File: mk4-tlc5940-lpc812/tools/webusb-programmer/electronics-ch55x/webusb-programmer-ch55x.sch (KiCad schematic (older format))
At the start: 19 parts, among them J1 USB_B_Micro, J2 Light Controller, Q1 PMV30UN, U1 CH552G, U3 STMPS2141STR

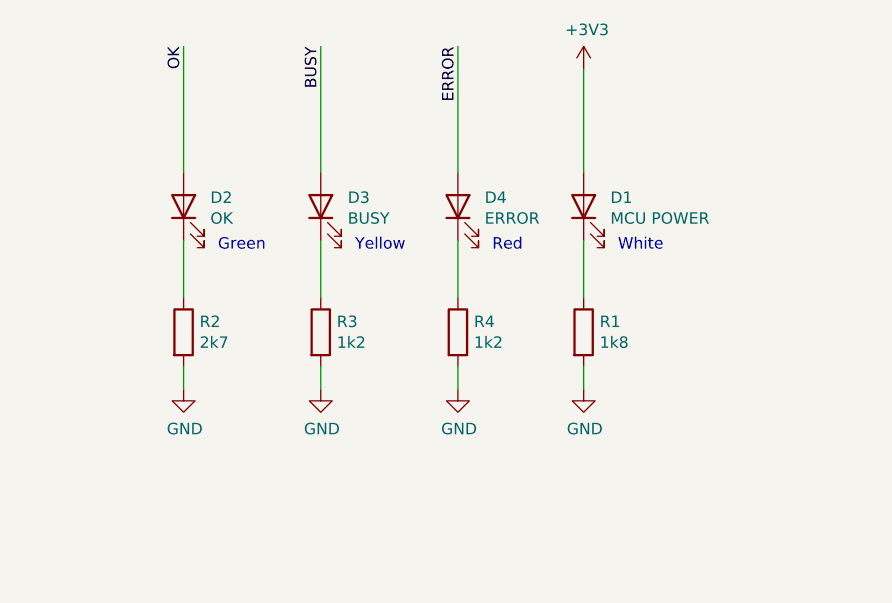
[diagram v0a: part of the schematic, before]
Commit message: Reverse LED polarity to prevent pull-up from lighting them up
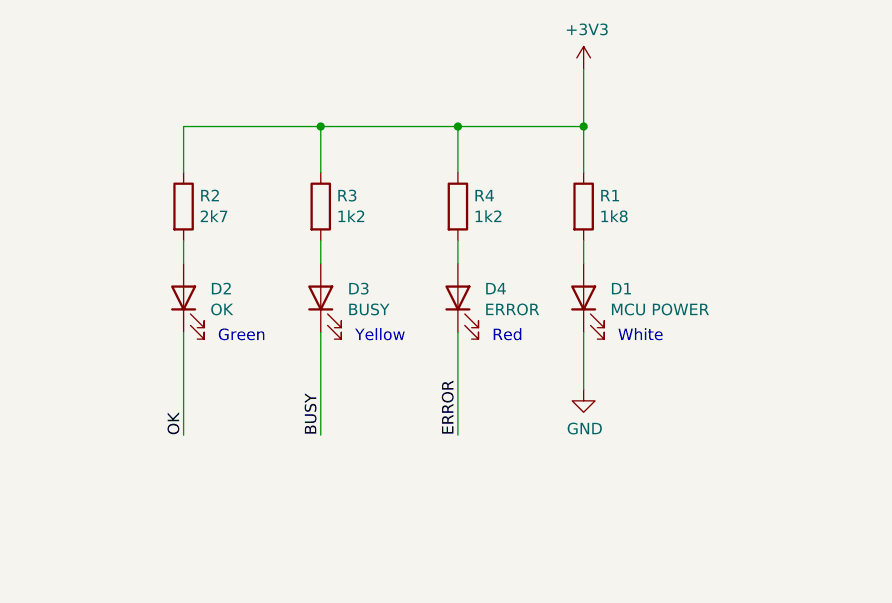
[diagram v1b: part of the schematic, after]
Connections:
- net +3V3: now also R1.1, R2.1, R3.1, R4.1; no longer D1.2 (A)
- net BUSY: now also D3.1 (K); no longer D3.2 (A)
- net ERROR: now also D4.1 (K); no longer D4.2 (A)
- net GND: now also D1.1 (K); no longer R1.2, R2.2, R3.2, R4.2
- net OK: now also D2.1 (K); no longer D2.2 (A)
- new net: D2.2 (A), R2.2
- new net: D3.2 (A), R3.2
- new net: D4.2 (A), R4.2
- new net: D1.2 (A), R1.2
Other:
- moved on the sheet: D1, D2, D3, D4, R1, R2, R3, R4
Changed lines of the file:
@@
 L Device:LED D2
 U 1 1 5E6F6F74
-P 3150 1800
-F 0 "D2" V 3189 1683 50  0000 R CNN
-F 1 "OK" V 3098 1683 50  0000 R CNN
-F 2 "WLA_LED_reverse_mount:LED_1204_reverse_mout" H 3150 1800 50  0001 C CNN
-F 3 "2011131907_TUOZHAN-TZ-P2-1204YGCTA1-1-5T" H 3150 1800 50  0001 C CNN
-F 4 "C91608" V 3150 1800 50  0001 C CNN "LCSC part number"
-	1    3150 1800
+P 3150 2200
+F 0 "D2" V 3189 2083 50  0000 R CNN
+F 1 "OK" V 3098 2083 50  0000 R CNN
+F 2 "WLA_LED_reverse_mount:LED_1204_reverse_mout" H 3150 2200 50  0001 C CNN
+F 3 "2011131907_TUOZHAN-TZ-P2-1204YGCTA1-1-5T" H 3150 2200 50  0001 C CNN
+F 4 "C91608" V 3150 2200 50  0001 C CNN "LCSC part number"
+	1    3150 2200
 	0    -1   -1   0
 $EndComp
@@
 L Device:LED D3
 U 1 1 5E6F790B
-P 3750 1800
-F 0 "D3" V 3789 1682 50  0000 R CNN
-F 1 "BUSY" V 3698 1682 50  0000 R CNN
-F 2 "WLA_LED_reverse_mount:LED_1204_reverse_mout" H 3750 1800 50  0001 C CNN
-F 3 "2009041237_TUOZHAN-TZ-P2-1204-0TA1-1-5T" H 3750 1800 50  0001 C CNN
-F 4 "C779805" V 3750 1800 50  0001 C CNN "LCSC part number"
-	1    3750 1800
+P 3750 2200
+F 0 "D3" V 3789 2082 50  0000 R CNN
+F 1 "BUSY" V 3698 2082 50  0000 R CNN
+F 2 "WLA_LED_reverse_mount:LED_1204_reverse_mout" H 3750 2200 50  0001 C CNN
+F 3 "2009041237_TUOZHAN-TZ-P2-1204-0TA1-1-5T" H 3750 2200 50  0001 C CNN
+F 4 "C779805" V 3750 2200 50  0001 C CNN "LCSC part number"
+	1    3750 2200
 	0    -1   -1   0
 $EndComp
@@
 L Device:LED D4
 U 1 1 5E6F7DEF
-P 4350 1800
-F 0 "D4" V 4389 1683 50  0000 R CNN
-F 1 "ERROR" V 4298 1683 50  0000 R CNN
-F 2 "WLA_LED_reverse_mount:LED_1204_reverse_mout" H 4350 1800 50  0001 C CNN
-F 3 "1905151403_MEIHUA-MHS110KECT" H 4350 1800 50  0001 C CNN
-F 4 "C389527" V 4350 1800 50  0001 C CNN "LCSC part number"
-	1    4350 1800
+P 4350 2200
+F 0 "D4" V 4389 2083 50  0000 R CNN
+F 1 "ERROR" V 4298 2083 50  0000 R CNN
+F 2 "WLA_LED_reverse_mount:LED_1204_reverse_mout" H 4350 2200 50  0001 C CNN
+F 3 "1905151403_MEIHUA-MHS110KECT" H 4350 2200 50  0001 C CNN
+F 4 "C389527" V 4350 2200 50  0001 C CNN "LCSC part number"
+	1    4350 2200
 	0    -1   -1   0
 $EndComp
@@
 L Device:LED D1
 U 1 1 5E6F89A9
-P 4900 1800
-F 0 "D1" V 4939 1683 50  0000 R CNN
-F 1 "MCU POWER" V 4848 1683 50  0000 R CNN
-F 2 "WLA_LED_reverse_mount:LED_1204_reverse_mout" H 4900 1800 50  0001 C CNN
-F 3 "2009041237_TUOZHAN-TZ-P2-1204WYS2-1-5T" H 4900 1800 50  0001 C CNN
-F 4 "C779804" V 4900 1800 50  0001 C CNN "LCSC part number"
-	1    4900 1800
+P 4900 2200
+F 0 "D1" V 4939 2083 50  0000 R CNN
+F 1 "MCU POWER" V 4848 2083 50  0000 R CNN
+F 2 "WLA_LED_reverse_mount:LED_1204_reverse_mout" H 4900 2200 50  0001 C CNN
+F 3 "2009041237_TUOZHAN-TZ-P2-1204WYS2-1-5T" H 4900 2200 50  0001 C CNN
+F 4 "C779804" V 4900 2200 50  0001 C CNN "LCSC part number"
+	1    4900 2200
 	0    -1   -1   0
 $EndComp
@@
 	10000 2850 10100 2850
 $Comp
-L power:GND #PWR014
-U 1 1 5E730E75
-P 3150 2600
-F 0 "#PWR014" H 3150 2350 50  0001 C CNN
-F 1 "GND" H 3155 2427 50  0000 C CNN
-F 2 "" H 3150 2600 50  0001 C CNN
-F 3 "" H 3150 2600 50  0001 C CNN
-	1    3150 2600
-	1    0    0    -1
-$EndComp
-$Comp
-L power:GND #PWR015
-U 1 1 5E73101A
-P 3750 2600
-F 0 "#PWR015" H 3750 2350 50  0001 C CNN
-F 1 "GND" H 3755 2427 50  0000 C CNN
-F 2 "" H 3750 2600 50  0001 C CNN
-F 3 "" H 3750 2600 50  0001 C CNN
-	1    3750 2600
-	1    0    0    -1
-$EndComp
-$Comp
-L power:GND #PWR016
-U 1 1 5E73121D
-P 4350 2600
-F 0 "#PWR016" H 4350 2350 50  0001 C CNN
-F 1 "GND" H 4355 2427 50  0000 C CNN
-F 2 "" H 4350 2600 50  0001 C CNN
-F 3 "" H 4350 2600 50  0001 C CNN
-	1    4350 2600
-	1    0    0    -1
-$EndComp
-$Comp
 L power:GND #PWR09
 U 1 1 5E73F918
@@
 Wire Wire Line
 	3700 4750 3700 4800
-Text Label 3150 1100 3    50   ~ 0
+Text Label 3150 2800 1    50   ~ 0
 OK
-Text Label 3750 1100 3    50   ~ 0
+Text Label 3750 2800 1    50   ~ 0
 BUSY
-Text Label 4350 1100 3    50   ~ 0
+Text Label 4350 2800 1    50   ~ 0
 ERROR
 Wire Wire Line
@@
 Text Notes 7850 2300 0    50   ~ 0
 High-side power switch,\nactive low
-Text Notes 5050 2000 0    50   ~ 0
+Text Notes 5050 2400 0    50   ~ 0
 White
-Text Notes 3300 2000 0    50   ~ 0
+Text Notes 3300 2400 0    50   ~ 0
 Green
-Text Notes 3900 2000 0    50   ~ 0
+Text Notes 3900 2400 0    50   ~ 0
 Yellow
-Text Notes 4500 2000 0    50   ~ 0
+Text Notes 4500 2400 0    50   ~ 0
 Red
 Text Notes 9750 3600 0    50   ~ 0
@@
 	4200 6550 4200 6200
 Wire Wire Line
-	4900 1950 4900 2200
-Wire Wire Line
-	4350 1950 4350 2200
-Wire Wire Line
-	3750 1950 3750 2200
-Wire Wire Line
-	3150 1950 3150 2200
+	4900 2350 4900 2600
+Wire Wire Line
+	4350 2350 4350 2800
+Wire Wire Line
+	3750 2350 3750 2800
+Wire Wire Line
+	3150 2350 3150 2800
 $Comp
 L Device:R R1
 U 1 1 5E6FD675
-P 4900 2350
-F 0 "R1" H 4970 2396 50  0000 L CNN
-F 1 "1k8" H 4970 2305 50  0000 L CNN
-F 2 "Resistor_SMD:R_0603_1608Metric_Pad1.05x0.95mm_HandSolder" V 4830 2350 50  0001 C CNN
-F 3 "~" H 4900 2350 50  0001 C CNN
-	1    4900 2350
+P 4900 1800
+F 0 "R1" H 4970 1846 50  0000 L CNN
+F 1 "1k8" H 4970 1755 50  0000 L CNN
+F 2 "Resistor_SMD:R_0603_1608Metric_Pad1.05x0.95mm_HandSolder" V 4830 1800 50  0001 C CNN
+F 3 "~" H 4900 1800 50  0001 C CNN
+	1    4900 1800
 	1    0    0    -1
 $EndComp
@@
 L Device:R R4
 U 1 1 5E6FC0B8
-P 4350 2350
-F 0 "R4" H 4420 2396 50  0000 L CNN
-F 1 "1k2" H 4420 2305 50  0000 L CNN
-F 2 "Resistor_SMD:R_0603_1608Metric_Pad1.05x0.95mm_HandSolder" V 4280 2350 50  0001 C CNN
-F 3 "~" H 4350 2350 50  0001 C CNN
-	1    4350 2350
+P 4350 1800
+F 0 "R4" H 4420 1846 50  0000 L CNN
+F 1 "1k2" H 4420 1755 50  0000 L CNN
+F 2 "Resistor_SMD:R_0603_1608Metric_Pad1.05x0.95mm_HandSolder" V 4280 1800 50  0001 C CNN
+F 3 "~" H 4350 1800 50  0001 C CNN
+	1    4350 1800
 	1    0    0    -1
 $EndComp
@@
 L Device:R R3
 U 1 1 5E6FBCF2
-P 3750 2350
-F 0 "R3" H 3820 2396 50  0000 L CNN
-F 1 "1k2" H 3820 2305 50  0000 L CNN
-F 2 "Resistor_SMD:R_0603_1608Metric_Pad1.05x0.95mm_HandSolder" V 3680 2350 50  0001 C CNN
-F 3 "~" H 3750 2350 50  0001 C CNN
-	1    3750 2350
+P 3750 1800
+F 0 "R3" H 3820 1846 50  0000 L CNN
+F 1 "1k2" H 3820 1755 50  0000 L CNN
+F 2 "Resistor_SMD:R_0603_1608Metric_Pad1.05x0.95mm_HandSolder" V 3680 1800 50  0001 C CNN
+F 3 "~" H 3750 1800 50  0001 C CNN
+	1    3750 1800
 	1    0    0    -1
 $EndComp
@@
 L Device:R R2
 U 1 1 5E6FABAC
-P 3150 2350
-F 0 "R2" H 3220 2396 50  0000 L CNN
-F 1 "2k7" H 3220 2305 50  0000 L CNN
-F 2 "Resistor_SMD:R_0603_1608Metric_Pad1.05x0.95mm_HandSolder" V 3080 2350 50  0001 C CNN
-F 3 "~" H 3150 2350 50  0001 C CNN
-	1    3150 2350
-	1    0    0    -1
-$EndComp
-Wire Wire Line
-	3150 2500 3150 2600
-Wire Wire Line
-	3750 2500 3750 2600
-Wire Wire Line
-	4350 2500 4350 2600
-Wire Wire Line
-	4900 2500 4900 2600
-Wire Wire Line
-	3150 1100 3150 1650
-Wire Wire Line
-	3750 1100 3750 1650
-Wire Wire Line
-	4350 1100 4350 1650
-Wire Wire Line
-	4900 1200 4900 1650
+P 3150 1800
+F 0 "R2" H 3220 1846 50  0000 L CNN
+F 1 "2k7" H 3220 1755 50  0000 L CNN
+F 2 "Resistor_SMD:R_0603_1608Metric_Pad1.05x0.95mm_HandSolder" V 3080 1800 50  0001 C CNN
+F 3 "~" H 3150 1800 50  0001 C CNN
+	1    3150 1800
+	1    0    0    -1
+$EndComp
+Wire Wire Line
+	3150 1950 3150 2050
+Wire Wire Line
+	3750 1950 3750 2050
+Wire Wire Line
+	4350 1950 4350 2050
+Wire Wire Line
+	4900 1950 4900 2050
+Wire Wire Line
+	3150 1450 3150 1650
+Wire Wire Line
+	3750 1450 3750 1650
+Wire Wire Line
+	4350 1450 4350 1650
+Wire Wire Line
+	4900 1200 4900 1450
+Wire Wire Line
+	3150 1450 3750 1450
+Connection ~ 4900 1450
+Wire Wire Line
+	4900 1450 4900 1650
+Connection ~ 3750 1450
+Wire Wire Line
+	3750 1450 4350 1450
+Connection ~ 4350 1450
+Wire Wire Line
+	4350 1450 4900 1450
 $EndSCHEMATC
